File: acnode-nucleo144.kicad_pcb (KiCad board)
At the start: 2 copper layers, 66 x 100 mm, 39 parts, among them J1 8P8C, J2 8P8C, J3 Conn_01x02, J4 Conn_01x03, J5 Conn_01x02, J6 Conn_01x04_Female, K1 SANYOU_SRD_Form_C, Q1 2N7002, Q2 2N7002, Q3 2N7002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

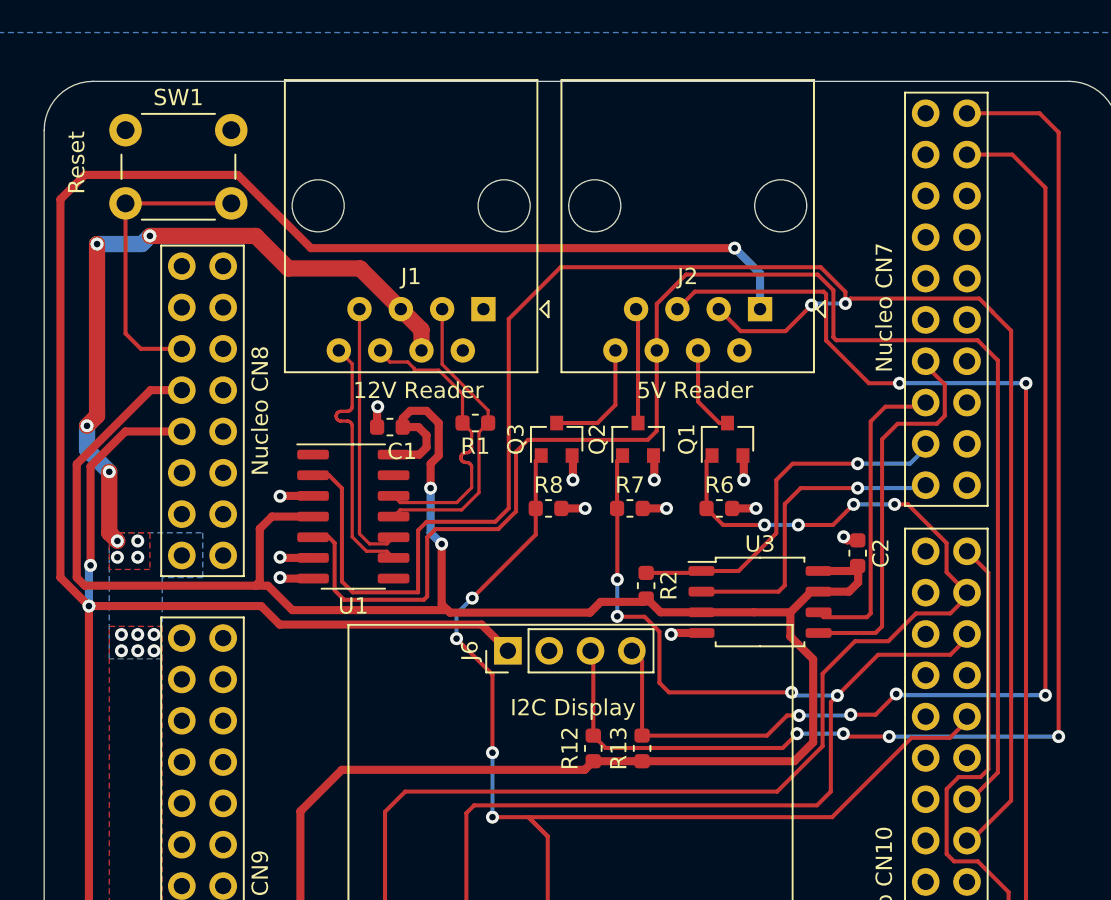
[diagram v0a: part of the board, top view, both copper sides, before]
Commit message: Switched to shielded 8P8C jack
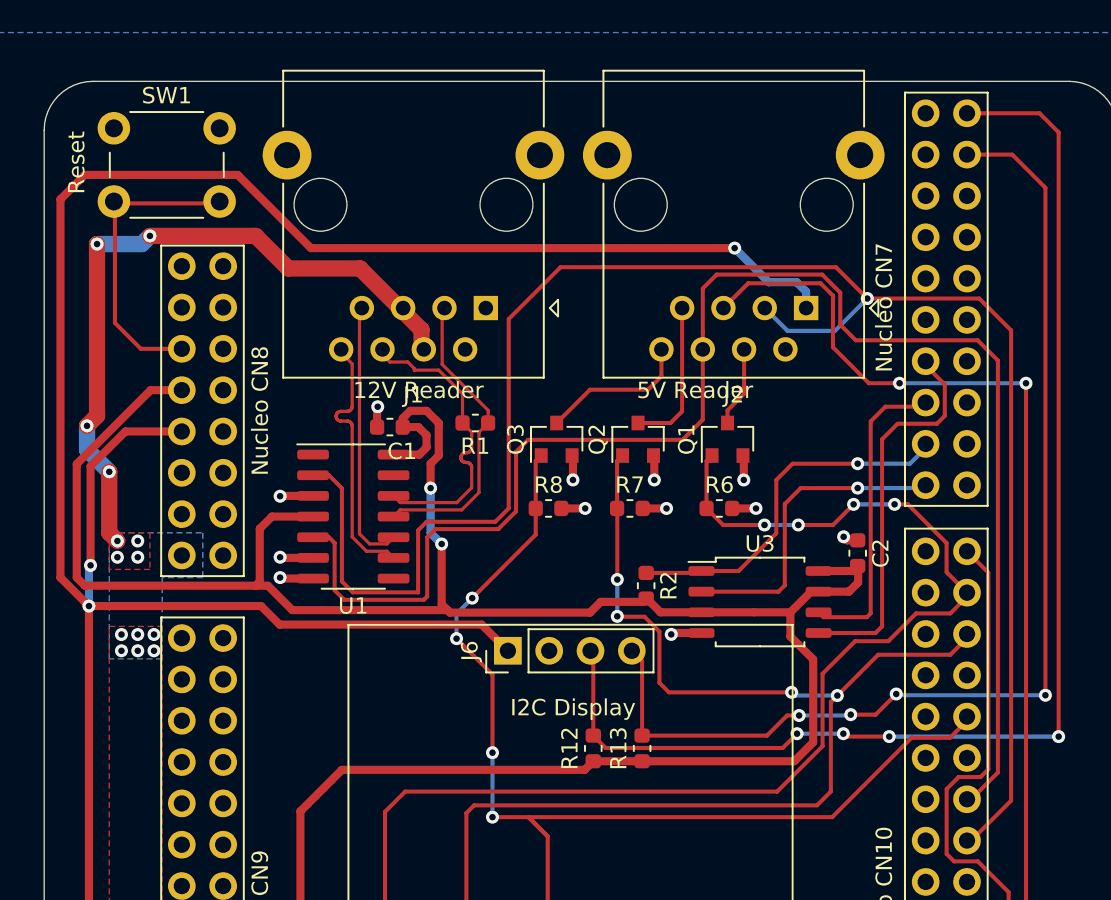
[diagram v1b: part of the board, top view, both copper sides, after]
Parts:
- J1, J2: value 8P8C -> 8P8C_Shielded; footprint Connector_RJ:RJ45_Amphenol_54602-x08_Horizontal -> Connector_RJ:RJ45_Ninigi_GE
- moved J2 2.83 mm to (160.8, 71.9)
- moved SW1 0.73 mm to (118.3, 60.9)
- moved J1 0.16 mm to (141.1, 71.9)
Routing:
- net /LED_Green_Cathode: track 7.05 -> 9.68 mm
- net BigButton: track 102.3 -> 100.1 mm
- net +5V: track 217.0 -> 219.1 mm
- net /Reader_SerialRx: track 110.6 -> 108.6 mm, vias 2 -> 1
- net /LED_Blue_Cathode: track 7.42 -> 9.28 mm
- net /LED_Red_Cathode: track 5.50 -> 4.95 mm

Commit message: Some changes I found on my computer
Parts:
- moved U3 0.10 mm to (157.9, 90.0)
- moved C2 0.08 mm to (163.9, 87.0)
- moved R2 0.05 mm to (151.1, 89.0)
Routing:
- net /LED_G_Trigger: track 77.9 -> 76.6 mm
- net GND: track 28.8 -> 29.4 mm

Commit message: I built one. Still obviously needs proper software support to fully test, but it doesn't look bad
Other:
- board text added: "ACNode Experimental Nucleo Board Michael Cullen Feb 2021"
- board text added: "THE Button"
